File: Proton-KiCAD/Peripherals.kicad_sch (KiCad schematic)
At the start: 41 parts, among them J8 HDMI_A, SW10 RIGHT_RIGHT, SW11 RIGHT_UP, SW12 RIGHT_DOWN, SW13 RIGHT_LEFT, SW6 LEFT_LEFT, SW7 LEFT_RIGHT, SW8 LEFT_UP, SW9 LEFT_DOWN, U11 MPU-6050

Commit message: Fixed to higherarchical labels
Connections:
- net GPIO21: no longer U11.1 (CLKIN), U11.11 (FSYNC), U11.12 (INT), U11.23 (SCL), U11.24 (SDA), U11.9 (AD0)
- new net IMU_AD0: U11.9 (AD0)
- new net IMU_CLK: U11.1 (CLKIN)
- new net IMU_FSYNC: U11.11 (FSYNC)
- new net IMU_INT: U11.12 (INT)
- new net IMU_SCL: U11.23 (SCL)
- new net IMU_SDA: U11.24 (SDA)
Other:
- moved on the sheet: J8
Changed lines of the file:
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@@
 	(wire
 		(pts
-			(xy 260.35 113.03) (xy 264.16 113.03)
+			(xy 260.35 113.03) (xy 265.43 113.03)
 		)
 		(stroke
@@
 		)
 	)
-	(label "GPIO21"
+	(hierarchical_label "IMU_FSYNC"
+		(shape input)
+		(at 68.58 153.67 180)
+		(effects
+			(font
+				(size 1.27 1.27)
+			)
+			(justify right)
+		)
+	)
+	(hierarchical_label "GPIO21"
+		(shape input)
 		(at 208.28 35.56 0)
 		(effects
@@
 				(size 1.27 1.27)
 			)
-			(justify left bottom)
-		)
-	)
-	(label "GPIO21"
+			(justify left)
+		)
+	)
+	(hierarchical_label "GPIO21"
+		(shape input)
+		(at 264.16 90.17 0)
+		(effects
+			(font
+				(size 1.27 1.27)
+			)
+			(justify left)
+		)
+	)
+	(hierarchical_label "IMU_AD0"
+		(shape input)
+		(at 68.58 146.05 180)
+		(effects
+			(font
+				(size 1.27 1.27)
+			)
+			(justify right)
+		)
+	)
+	(hierarchical_label "GPIO21"
+		(shape input)
+		(at 260.35 36.83 0)
+		(effects
+			(font
+				(size 1.27 1.27)
+			)
+			(justify left)
+		)
+	)
+	(hierarchical_label "IMU_SCL"
+		(shape input)
+		(at 68.58 143.51 180)
+		(effects
+			(font
+				(size 1.27 1.27)
+			)
+			(justify right)
+		)
+	)
+	(hierarchical_label "IMU_CLK"
+		(shape input)
+		(at 68.58 156.21 180)
+		(effects
+			(font
+				(size 1.27 1.27)
+			)
+			(justify right)
+		)
+	)
+	(hierarchical_label "GPIO21"
+		(shape input)
+		(at 265.43 113.03 0)
+		(effects
+			(font
+				(size 1.27 1.27)
+			)
+			(justify left)
+		)
+	)
+	(hierarchical_label "GPIO21"
+		(shape input)
+		(at 265.43 68.58 0)
+		(effects
+			(font
+				(size 1.27 1.27)
+			)
+			(justify left)
+		)
+	)
+	(hierarchical_label "IMU_INT"
+		(shape input)
+		(at 104.14 140.97 0)
+		(effects
+			(font
+				(size 1.27 1.27)
+			)
+			(justify left)
+		)
+	)
+	(hierarchical_label "GPIO21"
+		(shape input)
+		(at 212.09 113.03 0)
+		(effects
+			(font
+				(size 1.27 1.27)
+			)
+			(justify left)
+		)
+	)
+	(hierarchical_label "GPIO21"
+		(shape input)
+		(at 264.16 135.89 0)
+		(effects
+			(font
+				(size 1.27 1.27)
+			)
+			(justify left)
+		)
+	)
+	(hierarchical_label "GPIO21"
+		(shape input)
+		(at 212.09 135.89 0)
+		(effects
+			(font
+				(size 1.27 1.27)
+			)
+			(justify left)
+		)
+	)
+	(hierarchical_label "GPIO21"
+		(shape input)
+		(at 212.09 90.17 0)
+		(effects
+			(font
+				(size 1.27 1.27)
+			)
+			(justify left)
+		)
+	)
+	(hierarchical_label "IMU_SDA"
+		(shape input)
+		(at 68.58 140.97 180)
+		(effects
+			(font
+				(size 1.27 1.27)
+			)
+			(justify right)
+		)
+	)
+	(hierarchical_label "GPIO21"
+		(shape input)
 		(at 213.36 68.58 0)
 		(effects
@@
 				(size 1.27 1.27)
 			)
-			(justify left bottom)
-		)
-	)
-	(label "GPIO21"
-		(at 264.16 90.17 0)
-		(effects
-			(font
-				(size 1.27 1.27)
-			)
-			(justify left bottom)
-		)
-	)
-	(label "GPIO21"
-		(at 68.58 146.05 180)
-		(effects
-			(font
-				(size 1.27 1.27)
-			)
-			(justify right bottom)
-		)
-	)
-	(label "GPIO21"
-		(at 212.09 135.89 0)
-		(effects
-			(font
-				(size 1.27 1.27)
-			)
-			(justify left bottom)
-		)
-	)
-	(label "GPIO21"
-		(at 68.58 153.67 180)
-		(effects
-			(font
-				(size 1.27 1.27)
-			)
-			(justify right bottom)
-		)
-	)
-	(label "GPIO21"
-		(at 212.09 90.17 0)
-		(effects
-			(font
-				(size 1.27 1.27)
-			)
-			(justify left bottom)
-		)
-	)
-	(label "GPIO21"
-		(at 68.58 156.21 180)
-		(effects
-			(font
-				(size 1.27 1.27)
-			)
-			(justify right bottom)
-		)
-	)
-	(label "GPIO21"
-		(at 265.43 68.58 0)
-		(effects
-			(font
-				(size 1.27 1.27)
-			)
-			(justify left bottom)
-		)
-	)
-	(label "GPIO21"
-		(at 260.35 36.83 0)
-		(effects
-			(font
-				(size 1.27 1.27)
-			)
-			(justify left bottom)
-		)
-	)
-	(label "GPIO21"
-		(at 212.09 113.03 0)
-		(effects
-			(font
-				(size 1.27 1.27)
-			)
-			(justify left bottom)
-		)
-	)
-	(label "GPIO21"
-		(at 264.16 113.03 0)
-		(effects
-			(font
-				(size 1.27 1.27)
-			)
-			(justify left bottom)
-		)
-	)
-	(label "GPIO21"
-		(at 264.16 135.89 0)
-		(effects
-			(font
-				(size 1.27 1.27)
-			)
-			(justify left bottom)
-		)
-	)
-	(label "GPIO21"
-		(at 68.58 140.97 180)
-		(effects
-			(font
-				(size 1.27 1.27)
-			)
-			(justify right bottom)
-		)
-	)
-	(label "GPIO21"
-		(at 104.14 140.97 0)
-		(effects
-			(font
-				(size 1.27 1.27)
-			)
-			(justify left bottom)
-		)
-	)
-	(label "GPIO21"
-		(at 68.58 143.51 180)
-		(effects
-			(font
-				(size 1.27 1.27)
-			)
-			(justify right bottom)
+			(justify left)
 		)
 	)
@@
 	(symbol
 		(lib_id "Connector:HDMI_A")
-		(at 102.87 60.96 0)
+		(at 115.57 60.96 0)
 		(unit 1)
 		(body_style 1)
@@
 		(fields_autoplaced yes)
 		(property "Reference" "J8"
-			(at 114.3 59.6899 0)
+			(at 127 59.6899 0)
 			(show_name no)
 			(do_not_autoplace no)
@@
 		)
 		(property "Value" "HDMI_A"
-			(at 114.3 62.2299 0)
+			(at 127 62.2299 0)
 			(show_name no)
 			(do_not_autoplace no)
@@
 		)
 		(property "Footprint" ""
-			(at 103.505 60.96 0)
+			(at 116.205 60.96 0)
 			(hide yes)
 			(show_name no)
@@
 		)
 		(property "Datasheet" "https://en.wikipedia.org/wiki/HDMI"
-			(at 103.505 60.96 0)
+			(at 116.205 60.96 0)
 			(hide yes)
 			(show_name no)
@@
 		)
 		(property "Description" "HDMI type A connector"
-			(at 102.87 60.96 0)
-			(hide yes)
-			(show_name no)
+			(at 115.57 60.96 0)
+			(hide yes)
+			(show_name no)

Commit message: Added Battery Charger
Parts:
- added C55: 0.1u, Capacitor_SMD:C_0402_1005Metric, symbol Device:C
- added C56: 4.7u, Capacitor_SMD:C_0402_1005Metric, symbol Device:C
- added R18, R19: 1k, Resistor_SMD:R_0402_1005Metric, symbol Device:R_US
- added R53, R54: 1.13k, Resistor_SMD:R_0402_1005Metric, symbol Device:R_US
- added U5: BQ24072RGTR, BQ24072RGTR:IC_BQ24072RGTR, symbol BQ24072RGTR:BQ24072RGTR
- added UD5, UD6: BLUE, LED_SMD:LED_0805_2012Metric, symbol Device:LED
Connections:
- net +3V3: now also C56.1, R18.1, R19.1, U5.10 (OUT), U5.11 (OUT), U5.5 (EN2)
- net GND: now also C55.2, C56.2, R53.2, R54.2, U5.14 (TMR), U5.17 (EXP), U5.4 (~{CE}), U5.6 (EN1), U5.8 (VSS)
- new net: R54.1, U5.12 (ILIM)
- new net: R53.1, U5.16 (ISET)
- new net: U5.2 (BAT), U5.3 (BAT)
- new net: U5.7 (~{PGOOD}), UD6.1 (K)
- new net: U5.9 (~{CHG}), UD5.1 (K)
- new net: R18.2, UD5.2 (A)
- new net: R19.2, UD6.2 (A)
- new net SYSON: U5.15 (TD)
- new net UVBUS: C55.1, U5.13 (IN)
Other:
- moved on the sheet: J8

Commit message: Added Pinouts
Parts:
- added C57, C58: 100n, Capacitor_SMD:C_0402_1005Metric, symbol Device:C
- added J5: Conn_01x14_Pin, symbol Connector:Conn_01x14_Pin
- added R55, R57: 1k, Resistor_SMD:R_0402_1005Metric, symbol Device:R_US
- added R56, R58: 10k, Resistor_SMD:R_0402_1005Metric, symbol Device:R_US
- added SW14: LEFT_SEL, symbol Switch:SW_Push
- added SW15: RIGHT_SEL, symbol Switch:SW_Push
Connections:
- net +3V3: now also J5.1 (Pin_1), R55.1, R57.1
- net GND: now also C57.2, C58.2, J5.2 (Pin_2), R56.1, R58.1
- net VBUS: now reaches J8.18 (+5V)
- removed net GPIO21: C43.1, C44.1, C45.1, C46.1, C47.1, C48.1, C49.1, C50.1, R37.2, R39.2, R41.2, R43.2, R48.2, R49.2, R50.2, R51.2, RV1.2, RV2.2, SW10.2, SW11.2, SW12.2, SW13.2, SW6.2, SW7.2, SW8.2, SW9.2
- new net: R55.2, SW14.1
- new net: R57.2, SW15.1
- new net LEFT_DOWN: C46.1, R43.2, SW9.2
- new net LEFT_LEFT: C43.1, R37.2, SW6.2
- new net LEFT_RIGHT: C44.1, R39.2, SW7.2
- new net LEFT_SEL: C57.1, R56.2, SW14.2
- new net LEFT_SLIDE: RV1.2
- new net LEFT_UP: C45.1, R41.2, SW8.2
- new net RIGHT_DOWN: C49.1, R50.2, SW12.2
- new net RIGHT_LEFT: C50.1, R51.2, SW13.2
- new net RIGHT_RIGHT: C47.1, R48.2, SW10.2
- new net RIGHT_SEL: C58.1, R58.2, SW15.2
- new net RIGHT_SLIDE: RV2.2
- new net RIGHT_UP: C48.1, R49.2, SW11.2
- new net TFT_CS: J5.3 (Pin_3)
- new net TFT_LED: J5.8 (Pin_8)
- new net TFT_MISO: J5.9 (Pin_9)
- new net TFT_MOSI: J5.6 (Pin_6)
- new net TFT_RS: J5.5 (Pin_5)
- new net TFT_RST: J5.4 (Pin_4)
- new net TFT_SCK: J5.7 (Pin_7)
- new net TFT_T_CLK: J5.10 (Pin_10)
- new net TFT_T_CS: J5.11 (Pin_11)
- new net TFT_T_DIN: J5.12 (Pin_12)
- new net TFT_T_DO: J5.13 (Pin_13)
- new net TFT_T_IRQ: J5.14 (Pin_14)
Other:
- moved on the sheet: C43, C44, C45, C46, C47, C48, C49, C50, C51, C52, C53, C54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

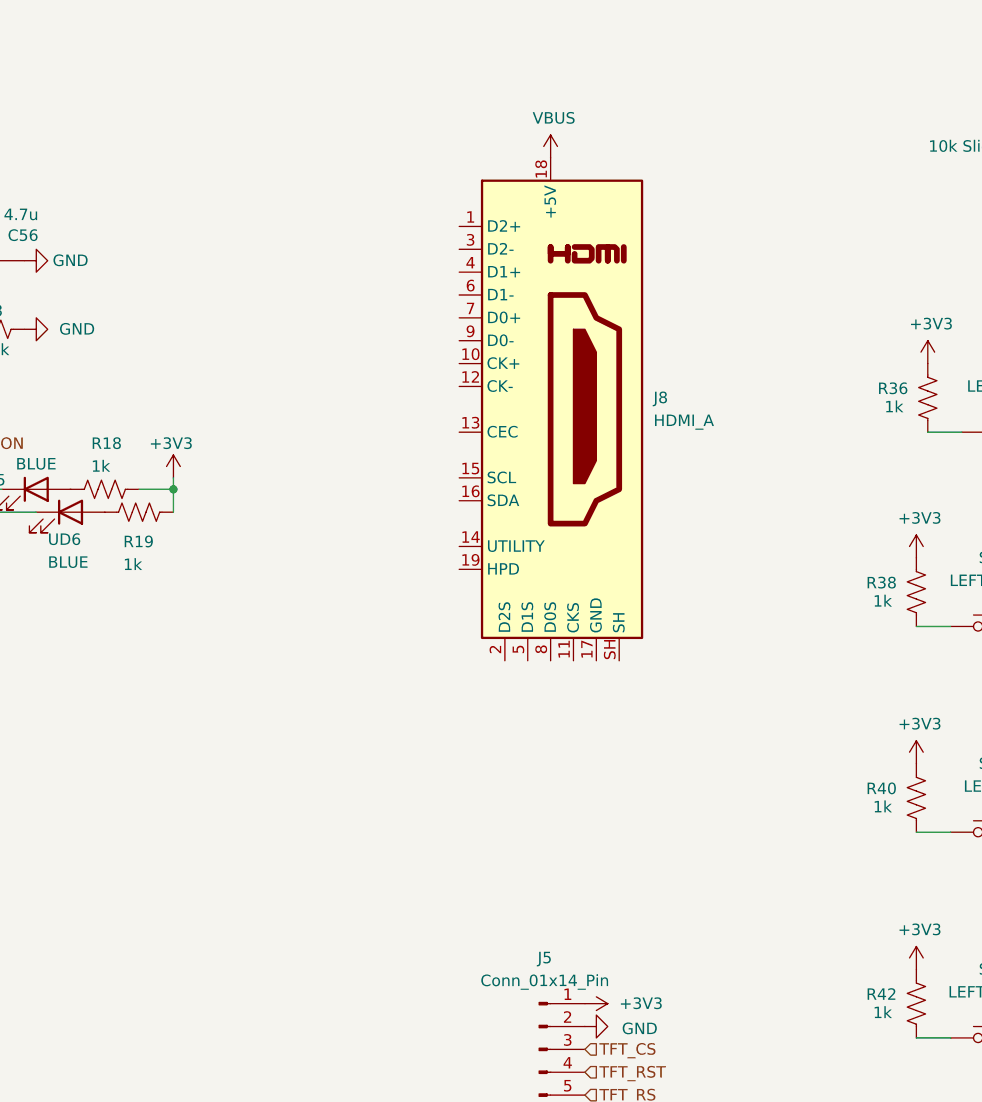
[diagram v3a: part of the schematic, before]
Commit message: Started layout
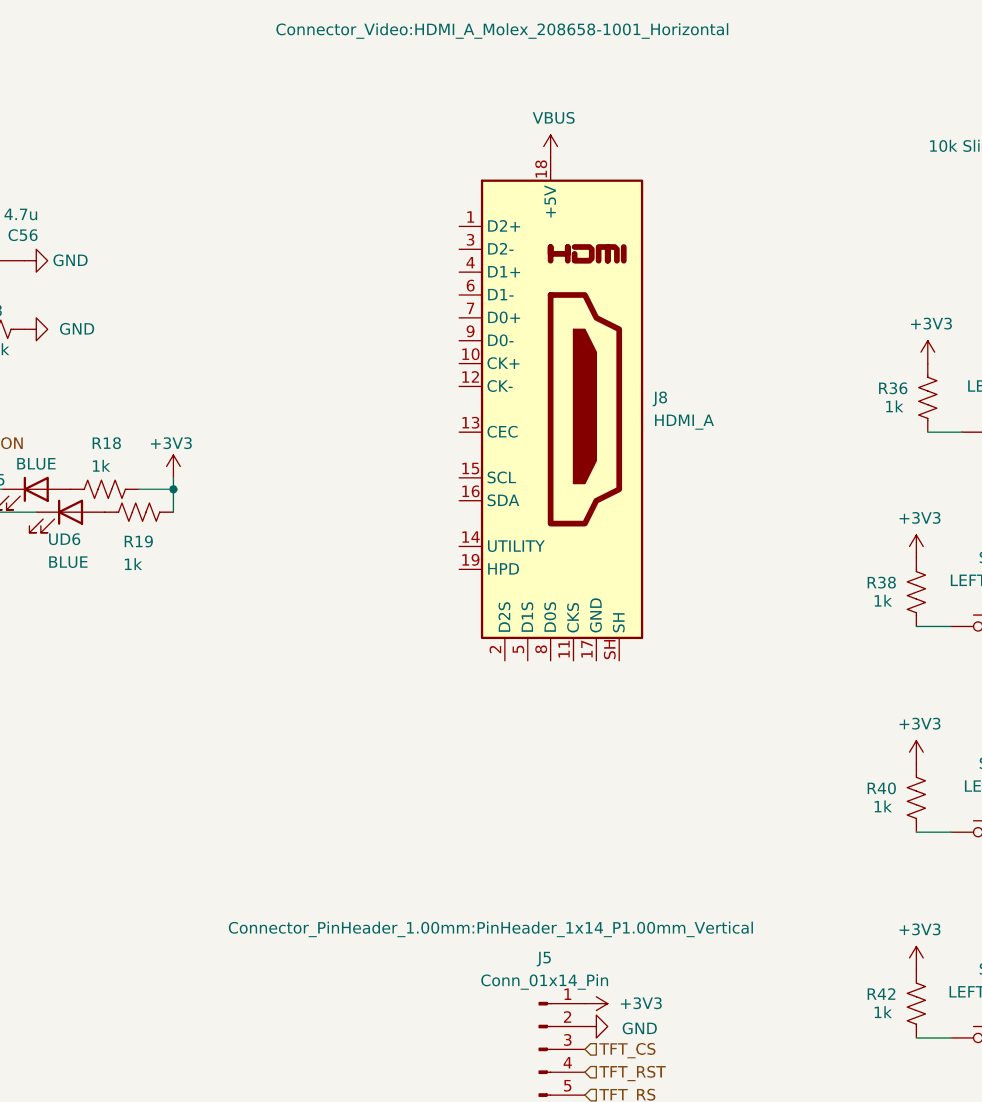
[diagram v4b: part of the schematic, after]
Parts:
- J5: footprint (none) -> Connector_PinHeader_1.00mm:PinHeader_1x14_P1.00mm_Vertical
- J8: footprint (none) -> Connector_Video:HDMI_A_Molex_208658-1001_Horizontal
- SW10, SW11, SW12, SW13, SW14, SW15, SW6, SW7, SW8, SW9: footprint (none) -> Button_Switch_THT:SW_PUSH-12mm
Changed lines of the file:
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@@
 			)
 		)
-		(property "Footprint" ""
+		(property "Footprint" "Button_Switch_THT:SW_PUSH-12mm"
 			(at 191.77 100.33 0)
 			(hide yes)
@@
 			)
 		)
-		(property "Footprint" ""
+		(property "Footprint" "Button_Switch_THT:SW_PUSH-12mm"
 			(at 243.84 100.33 0)
 			(hide yes)
@@
 		(in_pos_files yes)
 		(dnp no)
-		(fields_autoplaced yes)
 		(property "Reference" "J8"
 			(at 153.67 57.1499 0)
@@
 			)
 		)
-		(property "Footprint" ""
-			(at 142.875 58.42 0)
-			(hide yes)
+		(property "Footprint" "Connector_Video:HDMI_A_Molex_208658-1001_Horizontal"
+			(at 136.906 16.256 0)
 			(show_name no)
 			(do_not_autoplace no)
@@
 			)
 		)
-		(property "Footprint" ""
+		(property "Footprint" "Button_Switch_THT:SW_PUSH-12mm"
 			(at 243.84 123.19 0)
 			(hide yes)
@@
 			)
 		)
-		(property "Footprint" ""
+		(property "Footprint" "Button_Switch_THT:SW_PUSH-12mm"
 			(at 245.11 55.88 0)
 			(hide yes)
@@
 		(in_pos_files yes)
 		(dnp no)
-		(fields_autoplaced yes)
 		(property "Reference" "J5"
 			(at 141.605 119.38 0)
@@
 			)
 		)
-		(property "Footprint" ""
-			(at 140.97 139.7 0)
-			(hide yes)
+		(property "Footprint" "Connector_PinHeader_1.00mm:PinHeader_1x14_P1.00mm_Vertical"
+			(at 135.636 116.078 0)
 			(show_name no)
 			(do_not_autoplace no)
@@
 			)
 		)
-		(property "Footprint" ""
+		(property "Footprint" "Button_Switch_THT:SW_PUSH-12mm"
 			(at 243.84 77.47 0)
 			(hide yes)
@@
 			)
 		)
-		(property "Footprint" ""
+		(property "Footprint" "Button_Switch_THT:SW_PUSH-12mm"
 			(at 191.77 147.32 0)
 			(hide yes)
@@
 			)
 		)
-		(property "Footprint" ""
+		(property "Footprint" "Button_Switch_THT:SW_PUSH-12mm"
 			(at 191.77 123.19 0)
 			(hide yes)
@@
 			)
 		)
-		(property "Footprint" ""
+		(property "Footprint" "Button_Switch_THT:SW_PUSH-12mm"
 			(at 191.77 77.47 0)
 			(hide yes)
@@
 			)
 		)
-		(property "Footprint" ""
+		(property "Footprint" "Button_Switch_THT:SW_PUSH-12mm"
 			(at 243.84 147.32 0)
 			(hide yes)
@@
 			)
 		)
-		(property "Footprint" ""
+		(property "Footprint" "Button_Switch_THT:SW_PUSH-12mm"
 			(at 193.04 55.88 0)
 			(hide yes)
